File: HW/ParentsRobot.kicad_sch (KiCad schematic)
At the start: 26 parts, among them J1 Front_LEDs, J2 Screw_Terminal_01x02, J3 UART_BOOT, J4 LEFT_MOTORS, J5 RIGHT_MOTORS, Q1 BS170, SW1 SW_MEC_5G, SW2 SW_MEC_5G, SW3 ChannelSelection, U1 AMS1117-3.3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

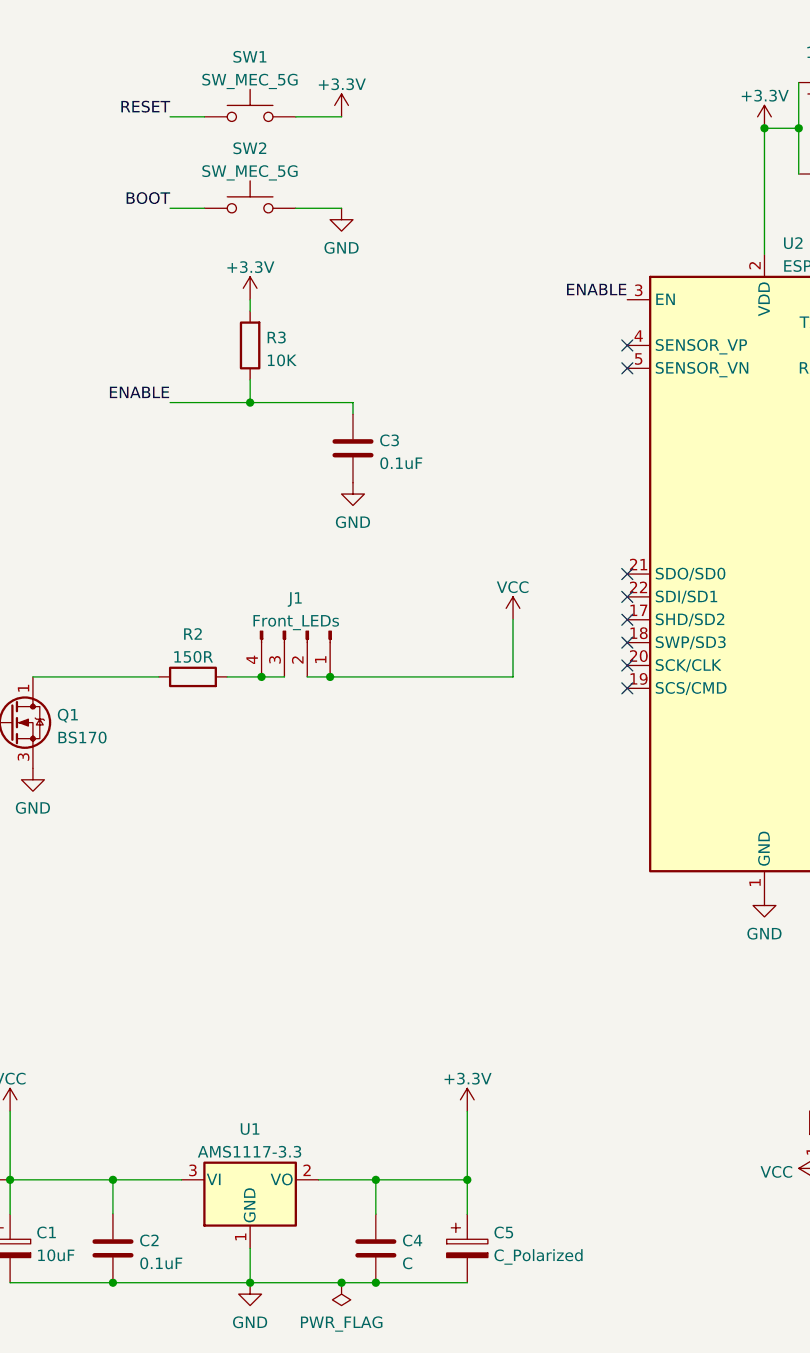
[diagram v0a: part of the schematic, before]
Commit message: Done schematic. Repaired wrong used buttons and connector for front leds + assigned footprints
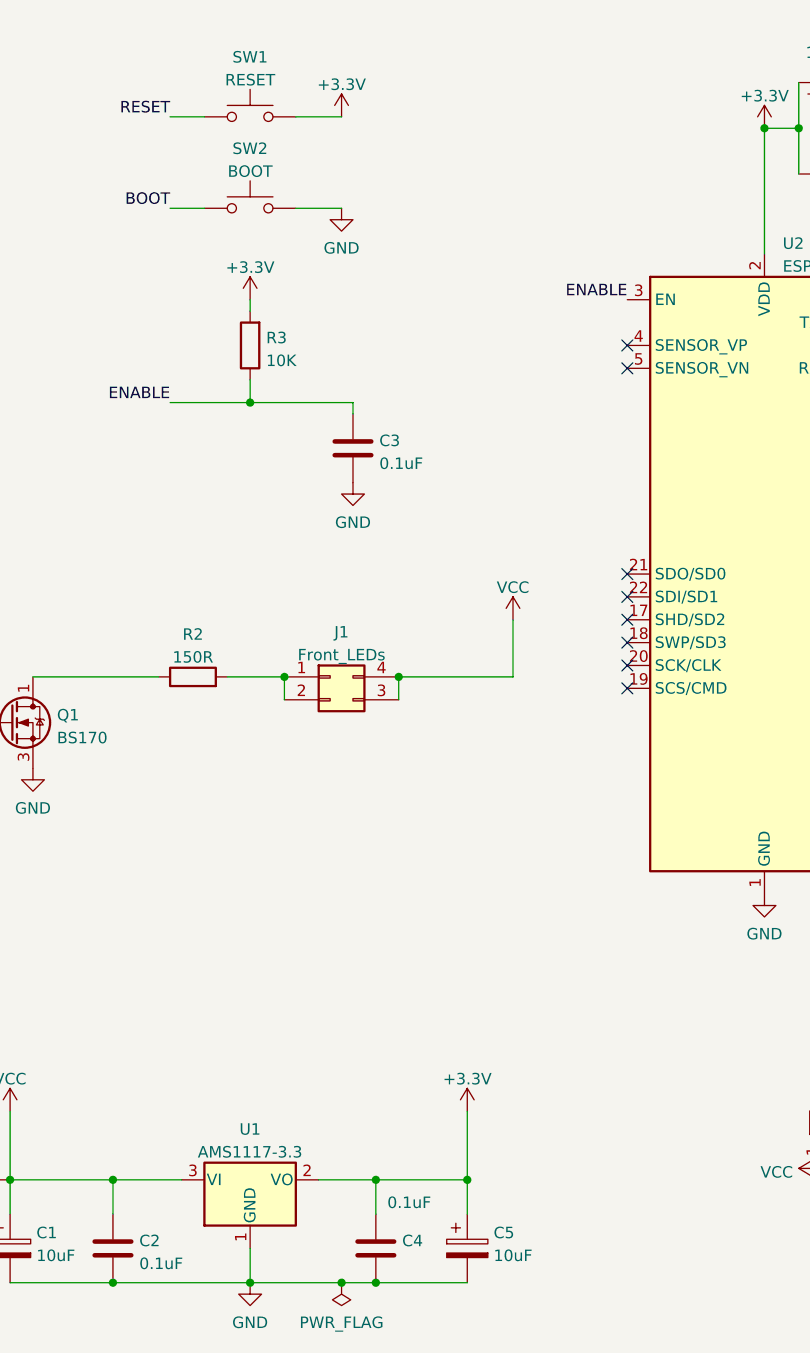
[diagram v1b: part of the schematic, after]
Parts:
- removed J1: Front_LEDs, symbol Connector:Conn_01x04_Male
- removed SW1, SW2: SW_MEC_5G, symbol Switch:SW_MEC_5G
- added J1: Front_LEDs, Connector_PinHeader_2.54mm:PinHeader_2x02_P2.54mm_Vertical, symbol Connector_Generic:Conn_02x02_Counter_Clockwise
- added SW1: RESET, Button_Switch_THT:SW_PUSH_6mm, symbol Switch:SW_Push
- added SW2: BOOT, Button_Switch_THT:SW_PUSH_6mm, symbol Switch:SW_Push
- C1, C6, C8: footprint (none) -> Capacitor_THT:CP_Radial_D4.0mm_P1.50mm
- C2, C3, C7, C9: footprint (none) -> Capacitor_THT:C_Disc_D5.0mm_W2.5mm_P5.00mm
- C4: value C -> 0.1uF; footprint (none) -> Capacitor_THT:C_Disc_D5.0mm_W2.5mm_P5.00mm
- C5: value C_Polarized -> 10uF; footprint (none) -> Capacitor_THT:CP_Radial_D4.0mm_P1.50mm
- D1: footprint (none) -> LED_THT:LED_D3.0mm_Clear
- J2, J4, J5: footprint (none) -> TerminalBlock:TerminalBlock_Altech_AK300-2_P5.00mm
- J3: footprint (none) -> Connector_PinHeader_2.54mm:PinHeader_1x04_P2.54mm_Vertical
- R1, R2, R3, R4: footprint (none) -> Resistor_THT:R_Axial_DIN0207_L6.3mm_D2.5mm_P7.62mm_Horizontal
- SW3: footprint (none) -> Button_Switch_THT:SW_DIP_SPSTx03_Slide_9.78x9.8mm_W7.62mm_P2.54mm
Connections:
- net +3V3: now also SW1.2
- net BOOT: now also SW2.1
- net GND: now also SW2.2
- net RESET: now also SW1.1
- net VCC: now also J1.3 (Pin_3), J1.4 (Pin_4)
- net at R2.2: now also J1.1 (Pin_1), J1.2 (Pin_2)

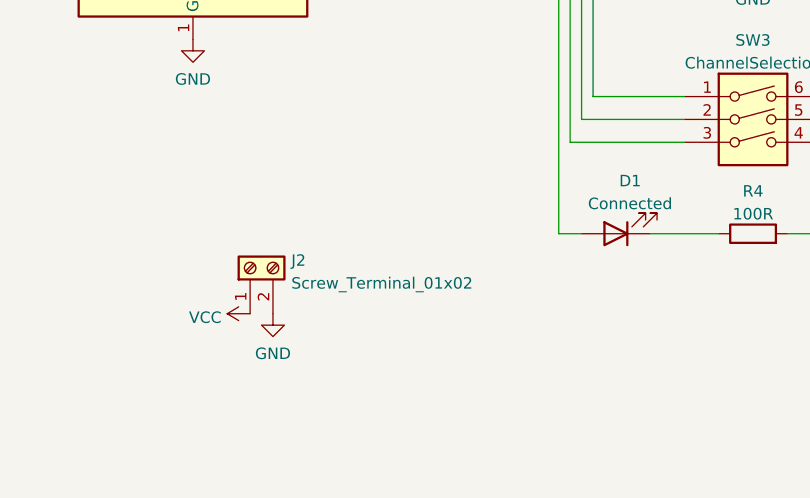
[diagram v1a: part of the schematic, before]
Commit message: Almost done PCB. Drill holes needs to be added
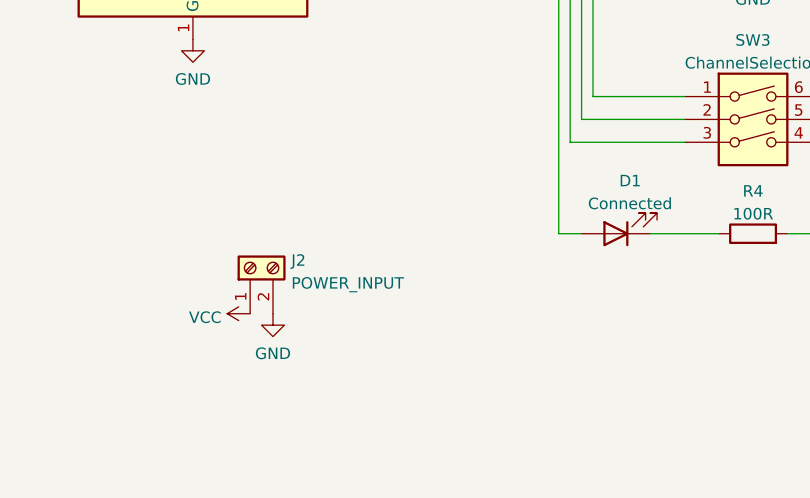
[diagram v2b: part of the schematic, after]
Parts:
- J2: value Screw_Terminal_01x02 -> POWER_INPUT
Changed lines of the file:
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@@
       (effects (font (size 1.27 1.27)) (justify right))
     )
-    (property "Value" "Screw_Terminal_01x02" (id 1) (at 145.542 137.5922 90)
+    (property "Value" "POWER_INPUT" (id 1) (at 145.542 137.5922 90)
       (effects (font (size 1.27 1.27)) (justify right))
     )
@@
     )
     (path "/3b9cb5ba-c1b2-45d6-95bc-60e5bf9b9564"
-      (reference "J2") (unit 1) (value "Screw_Terminal_01x02") (footprint "TerminalBlock:TerminalBlock_Altech_AK300-2_P5.00mm")
+      (reference "J2") (unit 1) (value "POWER_INPUT") (footprint "TerminalBlock:TerminalBlock_Altech_AK300-2_P5.00mm")
     )
     (path "/4500fcf3-cdd5-4b5a-aae6-530638779d64"

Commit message: Hardware done
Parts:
- added D2: D, Diode_THT:D_DO-41_SOD81_P7.62mm_Horizontal, symbol Device:D
- added H1, H2: MountingHole, MountingHole:MountingHole_3.2mm_M3, symbol Mechanical:MountingHole
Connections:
- net +3V3: now also D2.2 (A)
- net VCC: now also D2.1 (K)
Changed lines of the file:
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@@
+    (stroke (width 0) (type default) (color 0 0 0 0))
+  )
+  (wire (pts (xy 72.39 129.54) (xy 62.23 129.54))
     (stroke (width 0) (type default) (color 0 0 0 0))
   )
@@
     (stroke (width 0) (type default) (color 0 0 0 0))
   )
+  (wire (pts (xy 62.23 129.54) (xy 62.23 142.24))
+    (stroke (width 0) (type default) (color 0 0 0 0))
+  )
   (wire (pts (xy 204.47 119.38) (xy 212.09 119.38))
     (stroke (width 0) (type default) (color 0 0 0 0))
@@
     (stroke (width 0) (type default) (color 0 0 0 0))
   )
+  (wire (pts (xy 80.01 129.54) (xy 91.44 129.54))
+    (stroke (width 0) (type default) (color 0 0 0 0))
+  )
   (wire (pts (xy 146.05 20.32) (xy 146.05 25.4))
     (stroke (width 0) (type default) (color 0 0 0 0))
@@
   )
   (wire (pts (xy 209.55 71.12) (xy 222.25 71.12))
+    (stroke (width 0) (type default) (color 0 0 0 0))
+  )
+  (wire (pts (xy 91.44 129.54) (xy 91.44 142.24))
     (stroke (width 0) (type default) (color 0 0 0 0))
   )
@@
     )
     (pin "1")
+  )
+  (symbol (lib_id "Device:D") (at 76.2 129.54 0) (unit 1)
+    (in_bom yes) (on_board yes) (fields_autoplaced)
+    (property "Reference" "D2" (id 0) (at 76.2 124.5702 0))
+    (property "Value" "D" (id 1) (at 76.2 127.1071 0))
+    (property "Footprint" "Diode_THT:D_DO-41_SOD81_P7.62mm_Horizontal" (id 2) (at 76.2 129.54 0)
+      (effects (font (size 1.27 1.27)) hide)
+    )
+    (property "Datasheet" "~" (id 3) (at 76.2 129.54 0)
+      (effects (font (size 1.27 1.27)) hide)
+    )
+    (pin "1")
+    (pin "2")
   )
   (symbol (lib_id "Device:C") (at 62.23 149.86 0) (unit 1)
@@
     )
     (pin "1")
+  )
+  (symbol (lib_id "Mechanical:MountingHole") (at 60.96 114.3 0) (unit 1)
+    (in_bom yes) (on_board yes) (fields_autoplaced)
+    (property "Reference" "H2" (id 0) (at 63.5 113.4653 0)
+      (effects (font (size 1.27 1.27)) (justify left))
+    )
+    (property "Value" "MountingHole" (id 1) (at 63.5 116.0022 0)
+      (effects (font (size 1.27 1.27)) (justify left))
+    )
+    (property "Footprint" "MountingHole:MountingHole_3.2mm_M3" (id 2) (at 60.96 114.3 0)
+      (effects (font (size 1.27 1.27)) hide)
+    )
+    (property "Datasheet" "~" (id 3) (at 60.96 114.3 0)
+      (effects (font (size 1.27 1.27)) hide)
+    )
   )
   (symbol (lib_id "Transistor_FET:BS170") (at 50.8 91.44 0) (unit 1)
@@
     (pin "1")
   )
+  (symbol (lib_id "Mechanical:MountingHole") (at 35.56 114.3 0) (unit 1)
+    (in_bom yes) (on_board yes) (fields_autoplaced)
+    (property "Reference" "H1" (id 0) (at 38.1 113.4653 0)
+      (effects (font (size 1.27 1.27)) (justify left))
+    )
+    (property "Value" "MountingHole" (id 1) (at 38.1 116.0022 0)
+      (effects (font (size 1.27 1.27)) (justify left))
+    )
+    (property "Footprint" "MountingHole:MountingHole_3.2mm_M3" (id 2) (at 35.56 114.3 0)
+      (effects (font (size 1.27 1.27)) hide)
+    )
+    (property "Datasheet" "~" (id 3) (at 35.56 114.3 0)
+      (effects (font (size 1.27 1.27)) hide)
+    )
+  )
   (symbol (lib_id "Device:C") (at 91.44 149.86 0) (unit 1)
     (in_bom yes) (on_board yes)
@@
       (reference "D1") (unit 1) (value "Connected") (footprint "LED_THT:LED_D3.0mm_Clear")
     )
+    (path "/15a655d1-364b-4f69-aab5-353f56716d64"
+      (reference "D2") (unit 1) (value "D") (footprint "Diode_THT:D_DO-41_SOD81_P7.62mm_Horizontal")
+    )
+    (path "/ee7d5e7c-d3ab-4f11-9aac-84f9236ca843"
+      (reference "H1") (unit 1) (value "MountingHole") (footprint "MountingHole:MountingHole_3.2mm_M3")
+    )
+    (path "/6aeea2fd-eb38-43be-a239-e0d28acc3504"
+      (reference "H2") (unit 1) (value "MountingHole") (footprint "MountingHole:MountingHole_3.2mm_M3")
+    )
     (path "/ffaa9c49-d9fd-4dac-96a0-aa9e7884597f"
